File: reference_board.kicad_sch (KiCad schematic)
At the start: 15 parts, among them J1 Conn_02x05_Counter_Clockwise, U1 TMP236

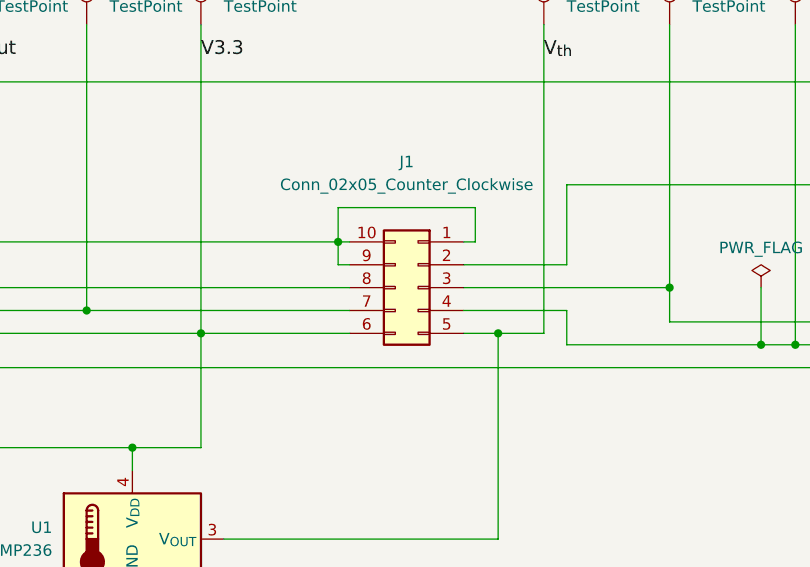
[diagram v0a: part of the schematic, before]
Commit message: Mirror the board-to-board connector to match a prototyp board.
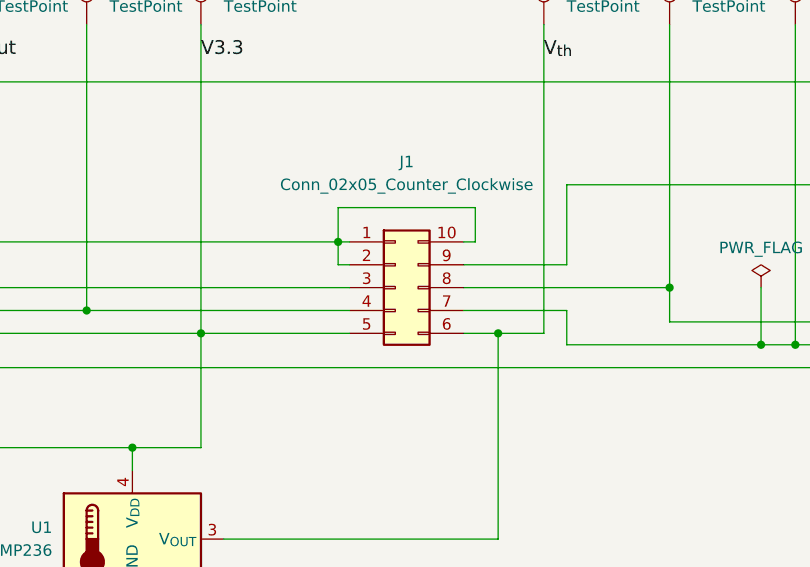
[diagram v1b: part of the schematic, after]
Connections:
- net GND: now also J1.2 (Pin_2); no longer J1.9 (Pin_9)
- net V3.3: now also J1.5 (Pin_5); no longer J1.6 (Pin_6)
- net V_{th}: now also J1.6 (Pin_6); no longer J1.5 (Pin_5)
- net Voltage Reference/V+: now also J1.7 (Pin_7); no longer J1.4 (Pin_4)
- net Voltage Reference/V-: now also J1.4 (Pin_4); no longer J1.7 (Pin_7)
- net Voltage Reference/V_zener+_force: now also J1.8 (Pin_8); no longer J1.3 (Pin_3)
- net Vout: now also J1.3 (Pin_3); no longer J1.8 (Pin_8)
- net Zener+_sense: now also J1.9 (Pin_9); no longer J1.2 (Pin_2)
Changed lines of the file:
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@@
 	(symbol
 		(lib_id "Connector_Generic:Conn_02x05_Counter_Clockwise")
-		(at 130.81 90.17 0)
-		(mirror y)
+		(at 128.27 90.17 0)
 		(unit 1)
 		(body_style 1)
@@
 		)
 		(property "Footprint" "Custom_footprints_project:Molex_SlimStack_53307-1071_2x05_P0.80mm_Vertical"
-			(at 130.81 90.17 0)
+			(at 128.27 90.17 0)
 			(hide yes)
 			(show_name no)
@@
 		)
 		(property "Datasheet" ""
-			(at 130.81 90.17 0)
+			(at 128.27 90.17 0)
 			(hide yes)
 			(show_name no)
@@
 		)
 		(property "Description" "Generic connector, double row, 02x05, counter clockwise pin numbering scheme (similar to DIP package numbering), script generated (kicad-library-utils/schlib/autogen/connector/)"
-			(at 130.81 90.17 0)
+			(at 128.27 90.17 0)
 			(hide yes)
 			(show_name no)
@@
 		)
 		(property "MFN" "Molex"
-			(at 130.81 90.17 0)
+			(at 128.27 90.17 0)
 			(hide yes)
 			(show_name no)
@@
 		)
 		(property "PN" "53307-1071"
-			(at 130.81 90.17 0)
+			(at 128.27 90.17 0)
 			(hide yes)
 			(show_name no)
@@
 		)
 		(property "RoHS" "Yes"
-			(at 130.81 90.17 0)
+			(at 128.27 90.17 0)
 			(hide yes)
 			(show_name no)
@@
 		)
 		(property "Temperature" "Tstorage = -40 °C to 105 °C"
-			(at 130.81 90.17 0)
+			(at 128.27 90.17 0)
 			(hide yes)
 			(show_name no)
